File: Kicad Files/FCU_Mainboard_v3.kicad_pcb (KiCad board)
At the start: 2 copper layers, 250 x 100 mm, 131 parts, among them J1 R_OLED, J10 AP2, J11 AP1, J12 BootLoader, J14 ALT_OLED, J15 VSPEED_OLED, J16 R_FD, J17 R_LS, J18 R_CSTR, J19 R_WPT, J2 L_OLED, J20 R_VORD, J21 R_NDB, J22 R_ARPT, J23 LB_PULL, J24 LB_PUSH, J25 LB_hPa/inHg, J26 L_FD, J27 L_LS, J28 L_CSTR, J29 L_WPT, J3 SPD_OLED, J30 SPD/MACH, J31 HDG/TRK, J32 MET_ALT, J33 LVL_OFF, J34 S_PUSH, J35 HDG_ENC, J36 RB_ENC, J37 H_PUSH, J38 RB_PULL, J39 RB_hPa/inHg, J4 HDG_OLED, J40 L_VORD, J41 SPD_ENC, J42 ALT_ENC, J43 A_PUSH, J44 RB_PUSH, J45 A_1H_1K, J46 VS_ENC, J47 L_NDB, J48 VS_PUSH, J49 RVOR/ADF_1, J5 H_T_OLED, J50 RVOR/ADF_2, J51 R_MAP_MODE, J52 L_ARPT, J53 R_MAP_RANGE, J54 L_MAP_MODE, J55 L_MAP_RANGE, J56 LB_ENC, J57 LVOR/ADF_1, J58 LVOR/ADF_2, J6 APPR, J69 S_PULL, J7 EXPED, J70 H_PULL, J71 A_PULL, J72 VS_PULL, J8 LOC, J9 A/THR, P1 USB_C_Plug_USB2.0, U1 CD74HC4067M, U2 CD74HC4067M, U3 CD74HC4067M, U4 CD74HC4067M, U5 ATMega2560, U6 CH340G, U7 AMS1117-3.3

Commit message: Fixed a serious error in the pcb design. I2C had a wrongly connected path between L an R EFIS OLEDs. Also added a dipswitch to select I2C address
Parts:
- removed D2: RX, LED_SMD:LED_1206_3216Metric_Pad1.42x1.75mm_HandSolder
- removed D3: TX, LED_SMD:LED_1206_3216Metric_Pad1.42x1.75mm_HandSolder
- removed R15, R16: 220, Resistor_SMD:R_1206_3216Metric_Pad1.30x1.75mm_HandSolder
- added R17: 10K, Resistor_SMD:R_1206_3216Metric_Pad1.30x1.75mm_HandSolder, F.Cu at (121.5, 50.0)
- added R18: 10K, Resistor_SMD:R_1206_3216Metric_Pad1.30x1.75mm_HandSolder, F.Cu at (121.5, 55.0)
- added R19: 10K, Resistor_SMD:R_1206_3216Metric_Pad1.30x1.75mm_HandSolder, F.Cu at (121.5, 59.5)
- added SW1: SW_DIP_x03, Button_Switch_THT:SW_DIP_SPSTx03_Slide_9.78x9.8mm_W7.62mm_P2.54mm, F.Cu at (107.4, 52.5)
- moved R24 2.12 mm to (133.6, 67.8)
- moved R6 1.93 mm to (156.9, 48.0)
- moved R25 1.87 mm to (156.9, 67.8)
- moved R23 1.62 mm to (133.6, 65.0)
- moved R3 1.55 mm to (133.7, 48.0)
- moved R26 1.42 mm to (156.9, 65.0)
- moved R5 1.19 mm to (157.0, 51.0)
- moved R22 1.17 mm to (133.6, 62.2)
- moved C1 1.08 mm to (148.6, 48.2)
- moved R20 1.08 mm to (142.5, 48.2)
- moved R2 1.03 mm to (133.7, 51.0)
- moved R28 0.92 mm to (156.9, 62.2)
- moved R29 0.78 mm to (156.9, 53.8)
- moved R21 0.72 mm to (133.6, 59.5)
- moved R1 0.53 mm to (133.7, 53.8)
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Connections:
- I2C_1 pad 1: GND -> /OLEDs/A0
- I2C_1 pad 2: GND -> /OLEDs/A1
- I2C_1 pad 21: GND -> /OLEDs/A2
- I2C_1 pad 4: /OLEDs/L_EFIS_SDA -> /OLEDs/R_EFIS_SDA
- I2C_1 pad 6: /OLEDs/R_EFIS_SDA -> /OLEDs/L_EFIS_SDA
- J1 pad 1: GND -> +3V3
- J1 pad 2: +3V3 -> GND
- J14 pad 1: GND -> +3V3
- J14 pad 2: +3V3 -> GND
- J15 pad 1: GND -> +3V3
- J15 pad 2: +3V3 -> GND
- J2 pad 1: GND -> +3V3
- J2 pad 2: +3V3 -> GND
- J3 pad 1: GND -> +3V3
- J3 pad 2: +3V3 -> GND
- J4 pad 1: GND -> +3V3
- J4 pad 2: +3V3 -> GND
- J5 pad 1: GND -> +3V3
- J5 pad 2: +3V3 -> GND
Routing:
- net R_EFIS_BARO_RIGHT: track 292.8 -> 146.7 mm, vias 1 -> 4
- net MP_S0: track 201.0 -> 308.4 mm, vias 6 -> 8
- net ALT_100: track 144.6 -> 212.6 mm, vias 1 -> 2
- net /OLEDs/A1: track 0.00 -> 65.7 mm, vias 0 -> 3
- net ALT_PUSH: track 90.5 -> 151.6 mm, vias 1 -> 3
- net L_EFIS_LS_LED: track 116.0 -> 176.5 mm, vias 2 -> 5
- net +5V: track 229.0 -> 288.5 mm, vias 4 -> 6
- net +3V3: track 545.1 -> 492.2 mm, vias 1 -> 3
- net HDG_RIGHT: track 138.0 -> 95.8 mm, vias 2 -> 1
- net /OLEDs/A2: track 0.00 -> 41.9 mm
- net /EFIS_LEFT/ARPT_BTN: track 137.2 -> 97.0 mm, vias 0 -> 1
- net ALT_LEFT: track 94.4 -> 133.5 mm, vias 1 -> 4
- net RXD: track 52.2 -> 15.3 mm, vias 2 -> 0
- net /OLEDs/R_EFIS_SCL: track 180.8 -> 144.1 mm, vias 1 -> 5
- net TXD: track 52.7 -> 16.4 mm, vias 2 -> 0
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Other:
- board text added: "A0"
- board text added: "A1"
- board text added: "A2"

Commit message: New routing with thicker 5V and 3V lines, better arrangement. Removed the useless RX and TX leds, they weren't really working as intended.
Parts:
- XT12MHz1, XT16MHz1: footprint Crystal:Crystal_SMD_EuroQuartz_MJ-4Pin_5.0x3.2mm_HandSoldering -> Crystal:Crystal_SMD_EuroQuartz_MQ-4Pin_7.0x5.0mm_HandSoldering
- moved XT16MHz1 6.64 mm to (177.3, 96.1)
- moved C14 4.62 mm to (178.0, 89.0)
- moved C13 4.09 mm to (178.0, 103.2)
- moved XT12MHz1 2.78 mm to (107.2, 94.2)
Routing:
- net A/THR_BTN: track 56.8 -> 116.1 mm, vias 1 -> 2
- net L_EFIS_LS_LED: track 176.5 -> 129.6 mm, vias 5 -> 3
- net RESET: track 83.4 -> 114.6 mm, vias 1 -> 2
- net MP_S0: track 308.4 -> 277.6 mm
- net MP_S2: track 260.8 -> 232.4 mm, vias 7 -> 8
- net R_EFIS_BARO_LEFT: track 165.8 -> 194.0 mm, vias 5 -> 3
- net R_EFIS_CSTR_LED: track 153.5 -> 125.9 mm, vias 4 -> 0
- net ALT_PUSH: track 151.6 -> 125.6 mm, vias 3 -> 2
- net R_EFIS_ARPT_LED: track 145.7 -> 171.4 mm, vias 1 -> 2
- net /OLEDs/L_EFIS_SDA: track 177.8 -> 152.8 mm
- net MP_S1: track 233.2 -> 208.6 mm
- net L_EFIS_FD_LED: track 129.0 -> 106.2 mm, vias 4 -> 0
- net Net-(U5-AREF): track 8.59 -> 30.0 mm, vias 0 -> 2
- net ALT_100: track 212.6 -> 193.7 mm
- net +5V: track 288.5 -> 270.3 mm
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
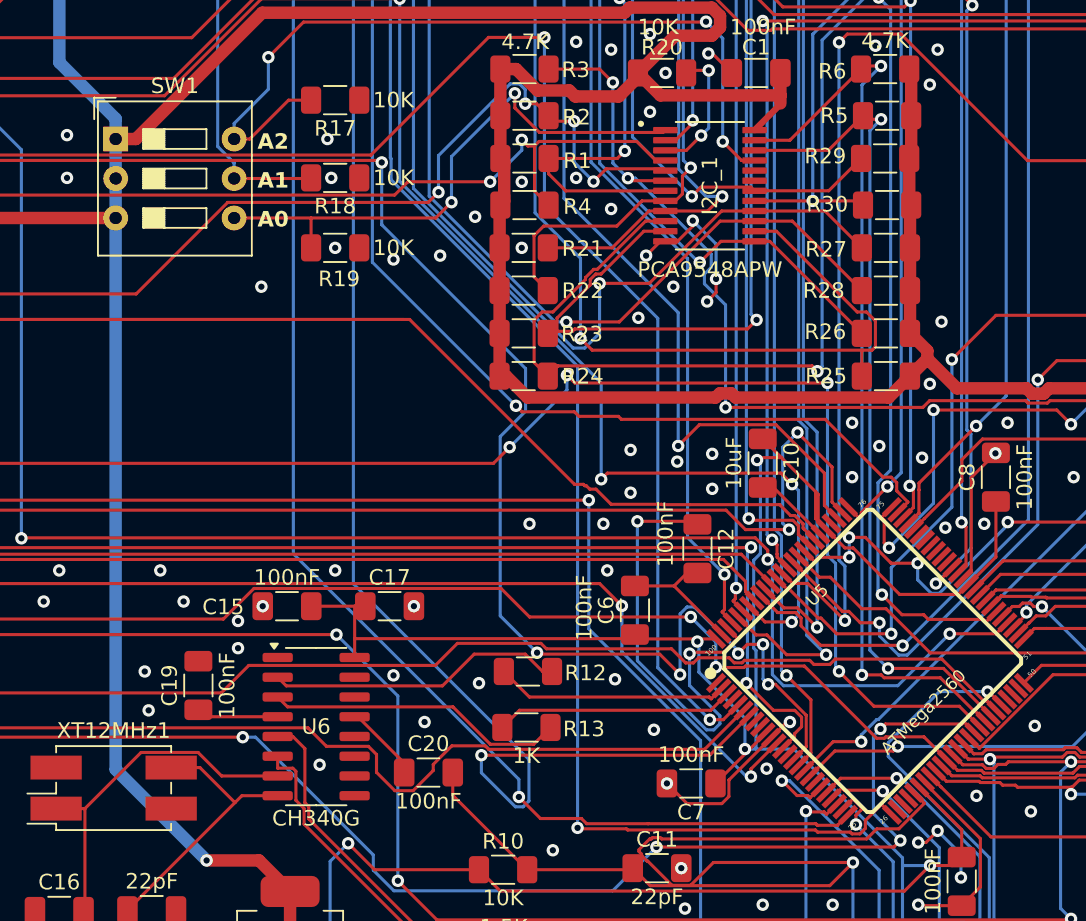
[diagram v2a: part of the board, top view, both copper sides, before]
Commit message: Complete rework of panels to be printed facedown. Important: change the order of the colors as Grey, White, Black, Transparent if using a Bambulab P1S/X1C ALso corrected some issue with the PCB (optional, you can print the FCU without using my pcb)
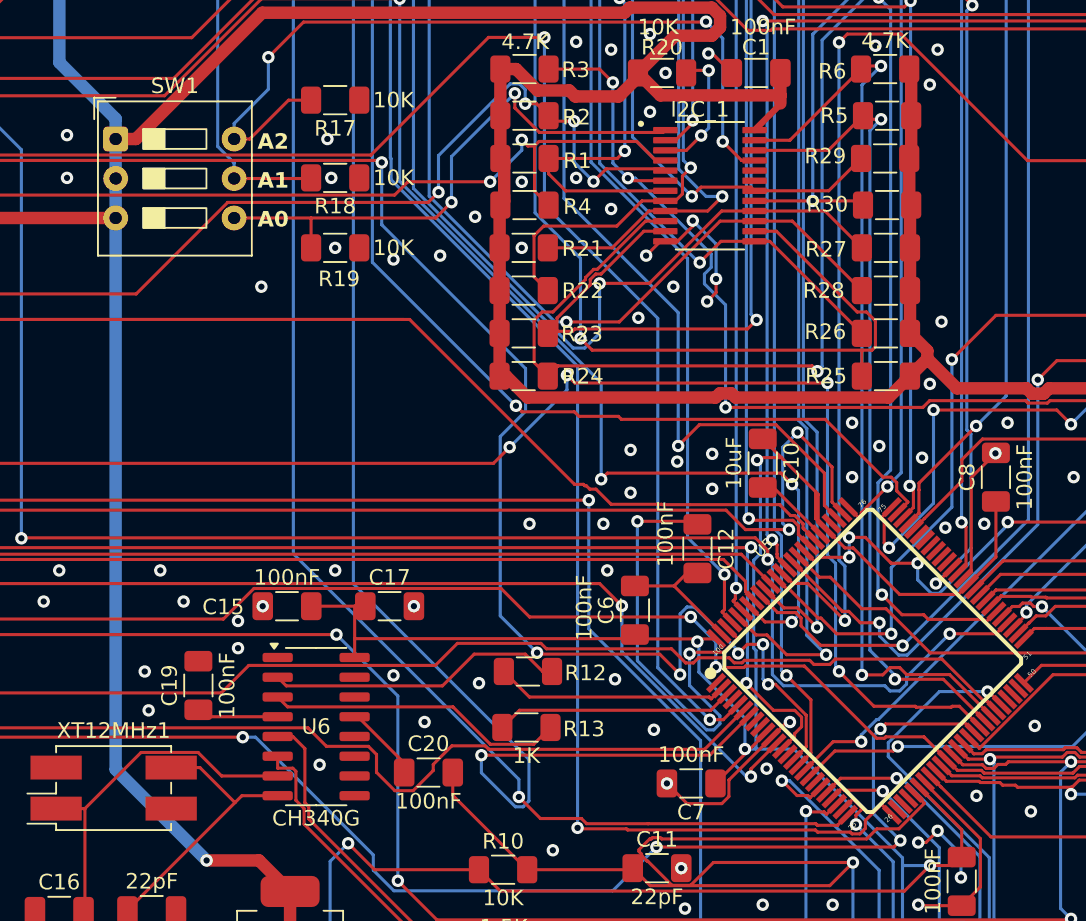
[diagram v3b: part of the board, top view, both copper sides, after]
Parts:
- I2C_1: footprint SFLibrary:SOP65P640X120-24N -> PCM_SFLibrary:SOP65P640X120-24N
- U5: footprint SFLibrary:TQFP100-0.5-14X14MM -> PCM_SFLibrary:TQFP100-0.5-14X14MM
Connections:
- U5 pad 43: SDA -> SCL
- U5 pad 44: SCL -> SDA
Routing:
- net SDA: track 59.0 -> 59.6 mm
- net ALT_PULL: track 119.4 -> 120.0 mm
